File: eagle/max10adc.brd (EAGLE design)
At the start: 98 x 62 mm, 205 parts, among them IC1 MAX19506, IC2 MAX19506, J1 MOLEX_BNC_73100-0105, J2 MOLEX_BNC_73100-0105, J3 MOLEX_BNC_73100-0105, J4 MOLEX_BNC_73100-0105, K1 AQY21SOP, K2 AQY21SOP, K3 AQY21SOP, K4 AQY21SOP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

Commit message: v8.8
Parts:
- removed C1, C2, C3, C4: 3-10pF, SparkFun-Passives:CTZ3
- removed CGAIN2_1, CGAIN2_2, CGAIN2_3, CGAIN2_4: 5pF, rcl@1:C0603
- removed C_S1, C_S2, C_S3, C_S4: 8-45pF, SparkFun-Passives:CTZ3
- added CH1, CH2, CH3, CH4: 3-10pF, SparkFun-Passives:CTZ3
- added CIN56_1, CIN56_2, CIN56_3, CIN56_4: 56pF, rcl@1:C0603
- added CL1, CL2, CL3, CL4: 8-45pF, SparkFun-Passives:CTZ3
- CGAIN1_1, CGAIN1_2, CGAIN1_3, CGAIN1_4: value 50pF -> 33pF
- CIN5_1, CIN5_2, CIN5_3, CIN5_4: value 5pF -> 10pF
- R_SCL, R_SDA: value 4.7k -> 10K
- SW_5V, SW_SUPER1, SW_SUPER2, SW_SUPER3, SW_SUPER4, SW_TERM1, SW_TERM2, SW_TERM3, SW_TERM4: value 0S102011MS2QS1 -> OS102011MS2QN1
- moved SW_RESET 60.8 mm to (48.8, 0.50), turned to 180 degrees
- moved R_SDA 22.3 mm to (15.0, 17.7)
- moved R_SCL 18.0 mm to (15.0, 19.8), turned to 0 degrees
- moved CIN5_4 7.80 mm to (63.9, 51.5)
- moved CIN5_1 7.60 mm to (63.8, 7.00)
- moved CIN5_3 7.06 mm to (64.9, 39.0)
- moved CIN5_2 7.02 mm to (64.9, 19.0)
- moved RGAIN1_3 4.61 mm to (68.4, 43.4), flipped to the bottom
- moved RGAIN3_3 4.61 mm to (70.5, 43.4), flipped to the bottom
- moved RGAIN3_4 4.61 mm to (68.4, 47.6), flipped to the bottom
- moved RGAIN2_3 4.51 mm to (64.0, 43.4), flipped to the bottom
- moved RGAIN4_3 4.49 mm to (66.2, 43.4), flipped to the bottom
- moved RGAIN1_2 4.10 mm to (69.0, 15.0), flipped to the bottom
- moved RGAIN3_2 4.10 mm to (71.1, 15.0), flipped to the bottom
- moved RGAIN1_1 4.10 mm to (69.0, 10.9), flipped to the bottom
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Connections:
- removed net N$42: CIN1NF_4.1, C_S4.+, RIN4_10K.1, SW_SUPER4.3
- new net N$36: CIN1NF_4.1, CIN56_4.1, RIN4_10K.1, SW_SUPER4.3
- net CGAIN1: now also CL1.-
- net CGAIN2: now also CH1.-; no longer CGAIN2_1.2
- net CGAIN3: now also CL2.-
- net CGAIN4: now also CH2.-; no longer CGAIN2_2.2
- net CGAIN5: now also CL3.-
- net CGAIN6: now also CH3.-; no longer CGAIN2_3.2
- net CGAIN7: now also CL4.-
- net CGAIN8: now also CH4.-; no longer CGAIN2_4.2
- net INAMINUS1: now also CH1.+, CIN56_1.2, CL1.+; no longer C1.-, CGAIN2_1.1, C_S1.-
- net INAMINUS2: now also CH3.+, CIN56_3.2, CL3.+; no longer C3.-, CGAIN2_3.1, C_S3.-
- net INBMINUS1: now also CH2.+, CIN56_2.2, CL2.+; no longer C2.-, CGAIN2_2.1, C_S2.-
- net INBMINUS2: now also CH4.+, CIN56_4.2, CL4.+; no longer C4.-, CGAIN2_4.1, C_S4.-
- net N$10: no longer C1.+
- net N$15: no longer C2.+
- net N$20: now also CIN56_1.1; no longer C_S1.+
- net N$38: now also CIN56_2.1; no longer C_S2.+
- net N$39: no longer C3.+
- net N$40: now also CIN56_3.1; no longer C_S3.+
- net N$41: no longer C4.+
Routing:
- net N$32: track 118.8 -> 147.1 mm
- net N$11: track 100.7 -> 127.0 mm
- net E_OVSAMP2: track 126.6 -> 103.1 mm, vias 2 -> 3
- net N$35: track 116.4 -> 137.3 mm, vias 5 -> 3
- net L124: track 53.8 -> 33.7 mm
- net NCONF: track 39.9 -> 57.3 mm
- net D0C: track 27.8 -> 12.2 mm
- net N$36: track 0.00 -> 14.9 mm
- net SERIALFROMLEFT_98: track 59.4 -> 44.8 mm, vias 2 -> 3
- net N$42: track 13.4 -> 0.00 mm
- net L21_SDA: track 94.0 -> 107.1 mm, vias 5 -> 6
- net L134: track 44.9 -> 57.4 mm, vias 2 -> 3
- net E_SHDN2: track 94.2 -> 81.8 mm, vias 2 -> 4
- net N$39: track 37.6 -> 26.1 mm, vias 1 -> 2
- net OFFSET4: track 43.0 -> 32.0 mm, vias 3 -> 2
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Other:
- board text added: "10pF"
- board text added: "1nF+56pF"
- board text added: "by Dr. Andy Haas"
- board text added: "high gain"
- board text added: "low gain"
- board text removed: "1nF"
- board text removed: "5pF"
- board text removed: "By Dr. Andy Haas"
- board text removed: "Super-gain"

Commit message: oshw logo
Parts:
- added GOLD_ORB_SM1: OSHWLOGOLOGO8MM, oshw:OSHW_8MM
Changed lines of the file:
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@@
 <?xml version="1.0" encoding="utf-8"?>
 <!DOCTYPE eagle SYSTEM "eagle.dtd">
-<eagle version="8.4.3">
+<eagle version="8.6.1">
 <drawing>
 <settings>
@@
 <param name="checkRestrict" value="1"/>
 <param name="checkStop" value="0"/>
+<param name="checkValues" value="0"/>
 <param name="useDiameter" value="13"/>
 <param name="maxErrors" value="999999"/>
@@
 <attribute name="MPN" value="06035A560FAT2A" x="60.3" y="51.1" size="1.778" layer="28" rot="MR180" display="off"/>
 </element>
+<element name="GOLD_ORB_SM1" library="oshw" package="OSHW_8MM" value="OSHWLOGOLOGO8MM" x="-1" y="39" rot="R90"/>
 </elements>
 <signals>

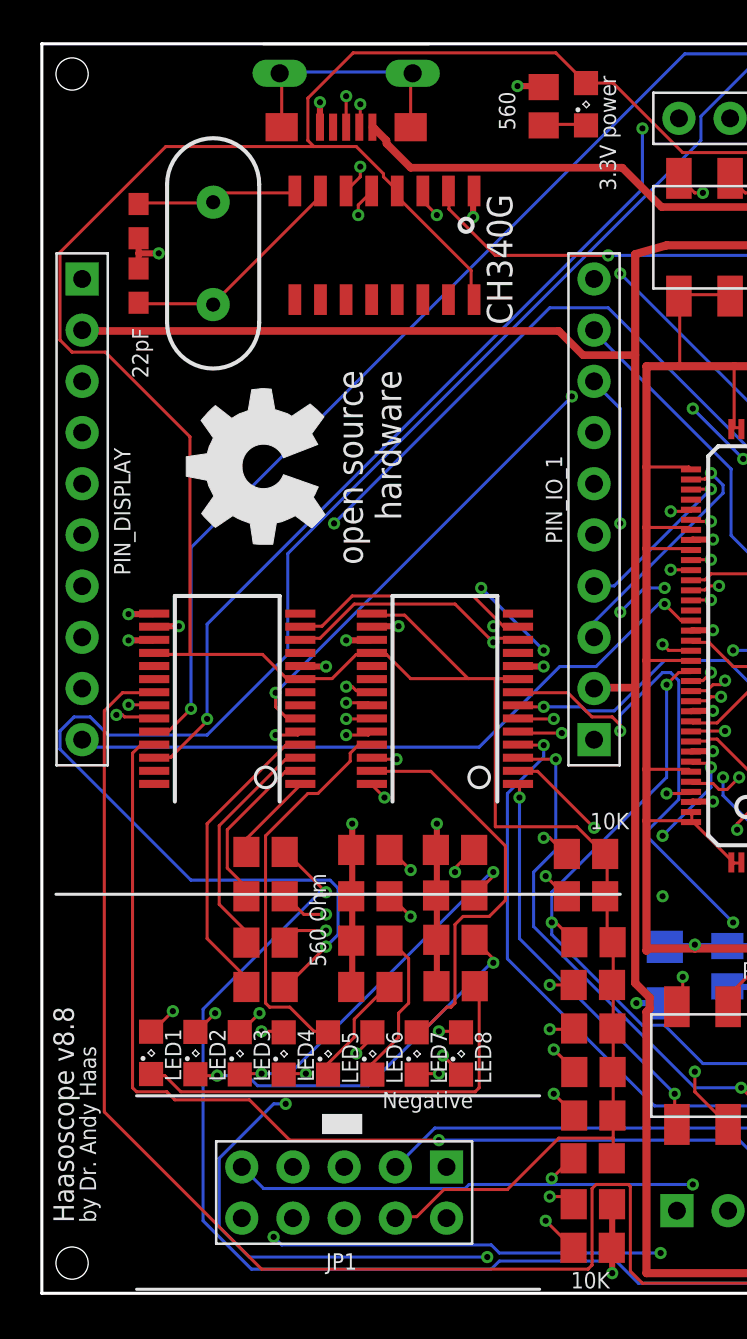
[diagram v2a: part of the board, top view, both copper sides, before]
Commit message: move USB to back of board
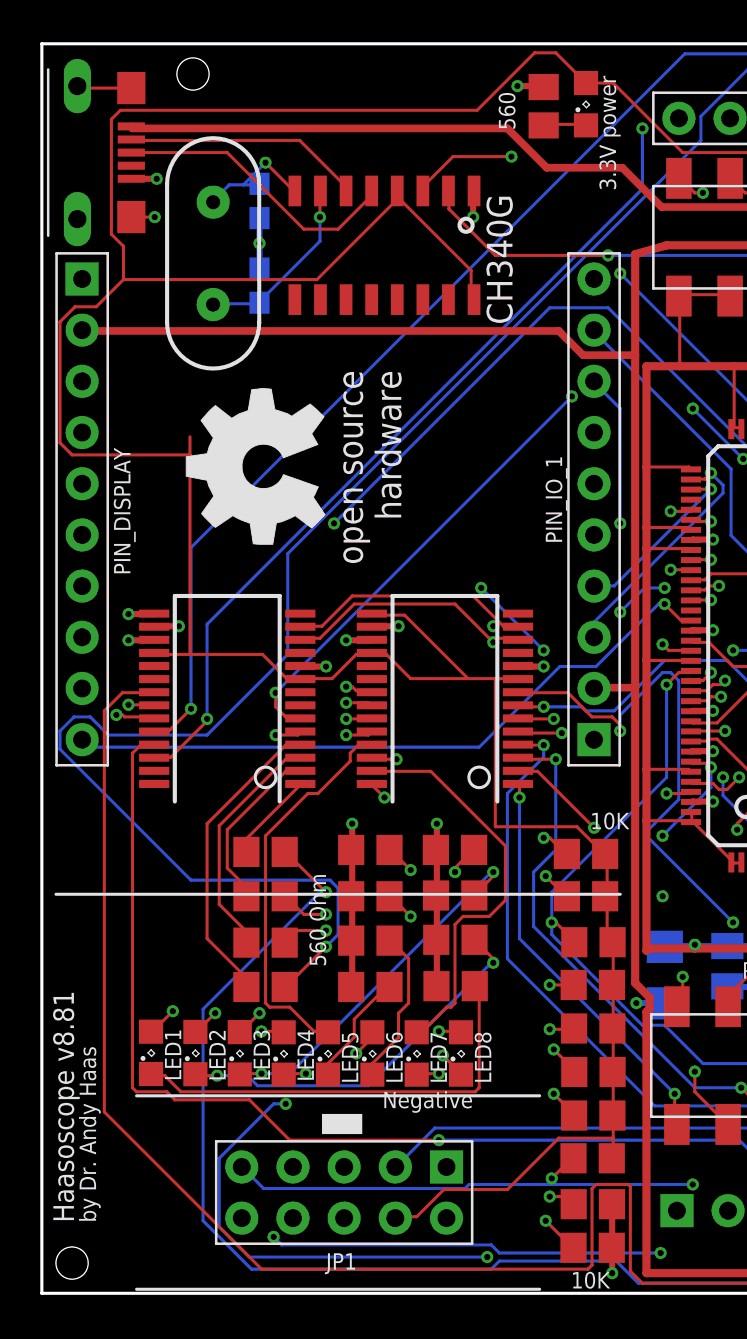
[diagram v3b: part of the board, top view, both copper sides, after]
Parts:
- moved USB1 13.7 mm to (-10.1, 54.6), turned to 270 degrees
- moved C_OSC2 6.08 mm to (-1.20, 52.2), flipped to the bottom
- moved C_OSC1 6.00 mm to (-1.20, 48.0), flipped to the bottom
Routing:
- net +3V3: track 424.7 -> 440.3 mm
- net 5VINFROMUSB: track 39.6 -> 51.5 mm
- net DMINUS: track 5.76 -> 11.9 mm, vias 2 -> 0
- net DPLUS: track 9.15 -> 14.4 mm, vias 2 -> 0
- net N$23: track 11.6 -> 9.18 mm, vias 0 -> 1
- net SLD: track 12.2 -> 14.4 mm, vias 0 -> 1
- net N$31: track 8.13 -> 6.33 mm, vias 0 -> 1
- net SERIALTORIGHT_RX_92: track 37.2 -> 36.1 mm
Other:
- board text added: "Haasoscope v8.81"
- board text removed: "Haasoscope v8.8"

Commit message: v8.81, 196 ordered on macrofab, labeled all pins
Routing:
- net +3V3: track 440.3 -> 437.3 mm
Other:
- board text added: "100"
- board text added: "101"
- board text added: "110"
- board text added: "111"
- board text added: "113"
- board text added: "114"
- board text added: "118"
- board text added: "119"
- board text added: "122"
- board text added: "124"
- board text added: "127"
- board text added: "130"
- board text added: "131"
- board text added: "132"
- board text added: "134"
- board text added: "135"
- board text added: "140"
- board text added: "29"
- board text added: "3.3V"
- board text added: "5V"
- board text added: "88"
- board text added: "89"
- board text added: "90"
- board text added: "91"
- board text added: "AIN1"
- board text added: "AIN14"
- board text added: "AIN6"
- board text added: "B0 E24"
- board text added: "E24 B7"
- board text added: "GND"
